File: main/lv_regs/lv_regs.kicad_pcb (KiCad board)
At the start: 2 copper layers, 176 x 67 mm, 53 parts, among them J1 Output, M1 ﻿APXW003A0X3-SRZ, M2 ﻿APXW003A0X3-SRZ, M3 ﻿APXW003A0X3-SRZ

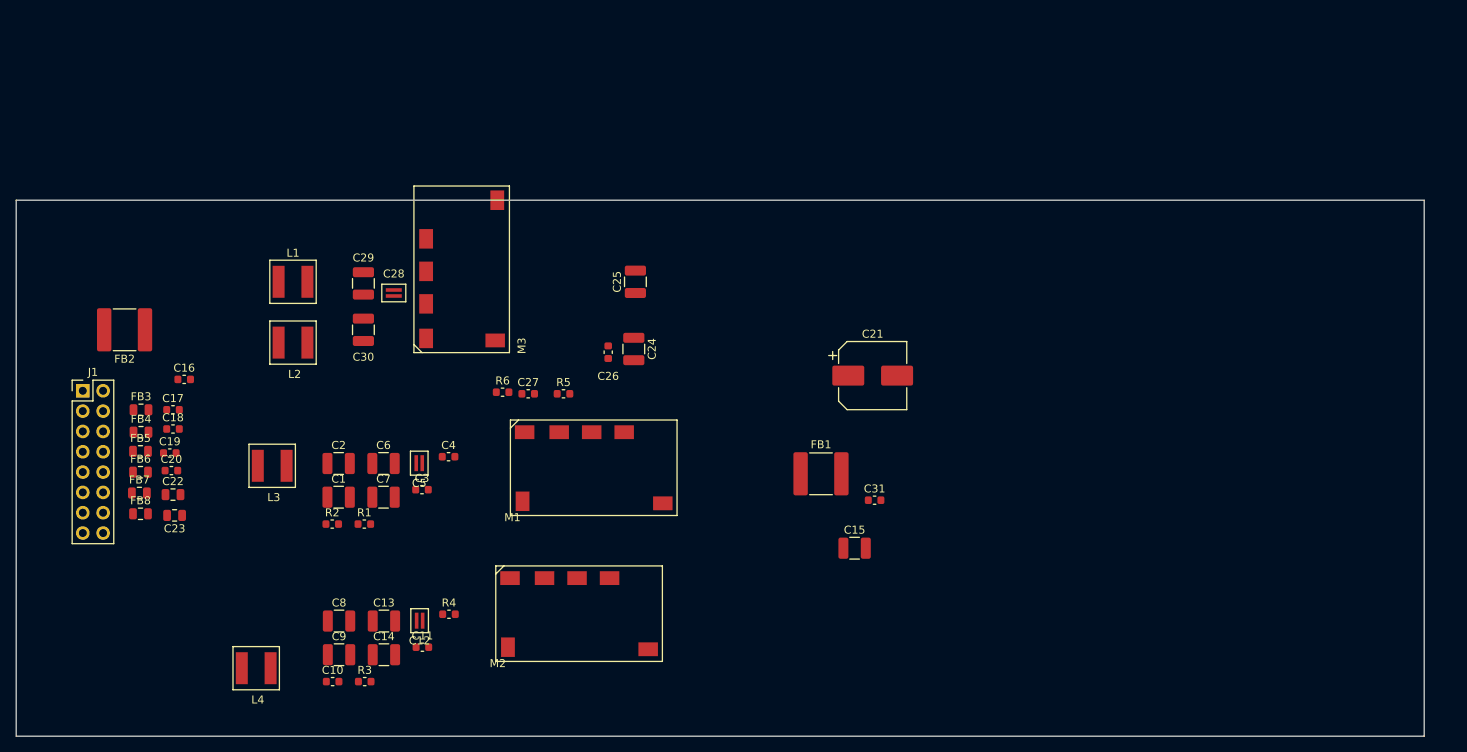
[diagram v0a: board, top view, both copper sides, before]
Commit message: A near final version of the low-volt regulator board. Pending footprint comparison on the actual parts.
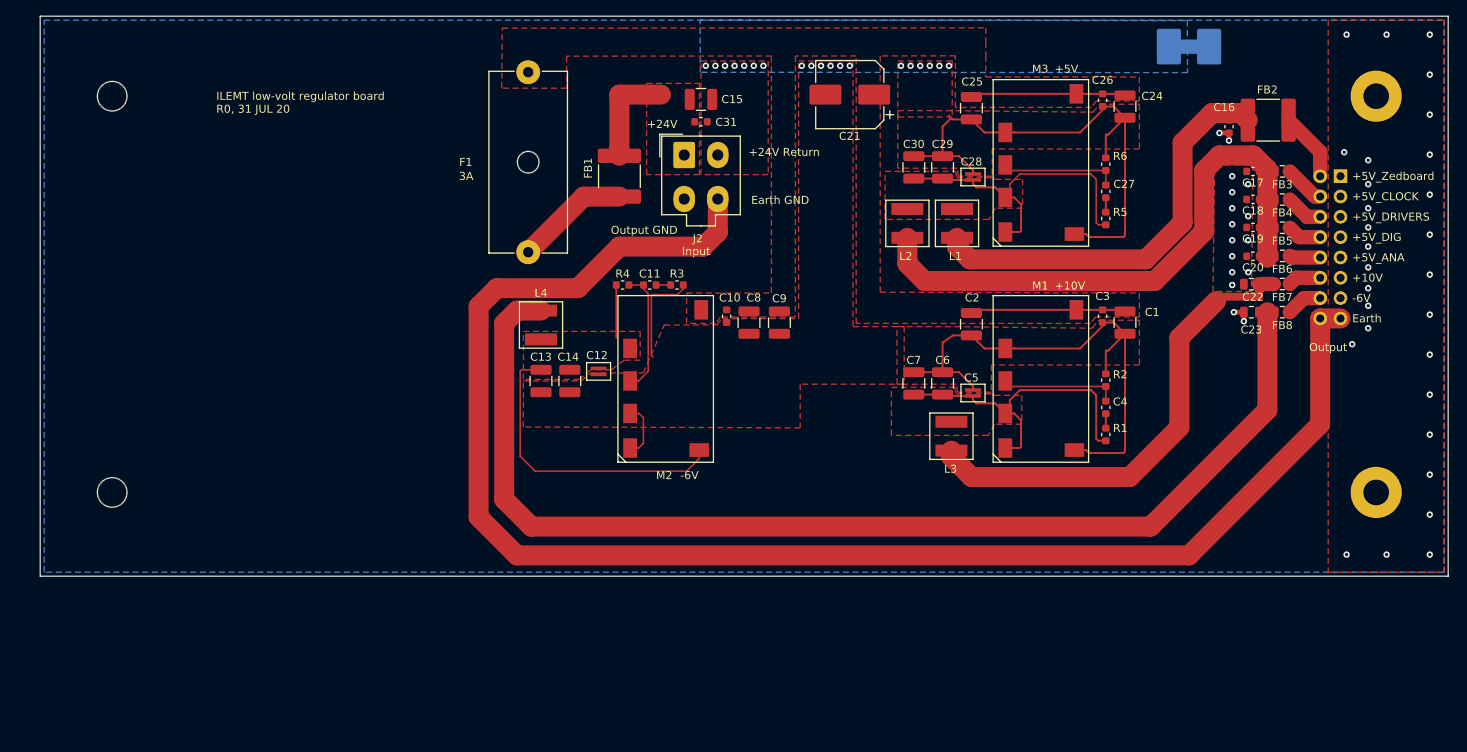
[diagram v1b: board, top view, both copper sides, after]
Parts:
- added F1: 3A, Fuse:Fuseholder_Cylinder-5x20mm_Schurter_0031_8201_Horizontal_Open, F.Cu at (94.0, 47.0)
- added J2: Input, Connector_Molex:Molex_Mini-Fit_Jr_5566-04A_2x02_P4.20mm_Vertical, F.Cu at (113.5, 57.4)
- added MH1: GND, MountingHole:MountingHole_3.2mm_M3_Pad, B.Cu at (200.0, 50.0)
- added MH2: GND, MountingHole:MountingHole_3.2mm_M3_Pad, B.Cu at (200.0, 99.5)
- added R7: DNP, Resistor_SMD:R_2816_7142Metric, B.Cu at (176.6, 43.8)
- added REF**: MountingHole_3.7mm, MountingHole:MountingHole_3.7mm, B.Cu at (42.0, 99.5)
- added REF**: MountingHole_3.7mm, MountingHole:MountingHole_3.7mm, B.Cu at (42.0, 50.0)
- C21: value 330uF -> 100uF
- J1: moved to B.Cu
- moved J1 159.5 mm to (195.5, 60.0), turned to 180 degrees
- moved FB3 145.7 mm to (188.3, 59.4), turned to 180 degrees
- moved FB4 145.6 mm to (188.3, 62.9), turned to 180 degrees
- moved FB5 145.4 mm to (188.3, 66.4), turned to 180 degrees
- moved FB2 145.3 mm to (186.5, 53.0), turned to 0 degrees
- moved FB6 145.3 mm to (188.3, 70.0), turned to 180 degrees
- moved FB7 145.2 mm to (188.3, 73.5), turned to 180 degrees
- moved FB8 144.9 mm to (188.3, 77.0), turned to 180 degrees
- moved C19 138.3 mm to (184.6, 66.4), turned to 180 degrees
- moved C17 138.2 mm to (184.6, 59.4), turned to 180 degrees
- moved C18 138.0 mm to (184.6, 62.9), turned to 180 degrees
- moved C20 137.8 mm to (184.6, 70.0), turned to 180 degrees
- moved C22 137.3 mm to (184.4, 73.5)
- moved C23 137.0 mm to (184.4, 77.0), turned to 0 degrees
- moved C16 134.4 mm to (181.6, 53.8), turned to 270 degrees
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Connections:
- net /reg -5V/VOUT renamed /reg +5V/VOUT
- net Net-(C16-Pad1) renamed /FILT_5V_ZED
- net Net-(C22-Pad2) renamed /FILT_10V
- net Net-(C23-Pad2) renamed /FILT_-6V
- C1 pad 2: GND -> GNDPWR
- C10 pad 2: GND -> GNDPWR
- C12 pad 1: GND -> GNDPWR
- C13 pad 1: GND -> GNDPWR
- C14 pad 1: GND -> GNDPWR
- C15 pad 1: GND -> GNDPWR
- C17 pad 1: Net-(C17-Pad1) -> /FILT_5V_OTHER
- C18 pad 1: Net-(C18-Pad1) -> /FILT_5V_OTHER
- C19 pad 1: Net-(C19-Pad1) -> /FILT_5V_OTHER
- C2 pad 2: GND -> GNDPWR
- C20 pad 1: Net-(C20-Pad1) -> /FILT_5V_OTHER
- C21 pad 2: GND -> GNDPWR
- C24 pad 2: GND -> GNDPWR
- C25 pad 2: GND -> GNDPWR
- C26 pad 2: GND -> GNDPWR
- C28 pad 2: GND -> GNDPWR
- C29 pad 2: GND -> GNDPWR
- C3 pad 2: GND -> GNDPWR
- C30 pad 2: GND -> GNDPWR
- C31 pad 2: GND -> GNDPWR
- C5 pad 2: GND -> GNDPWR
- C6 pad 2: GND -> GNDPWR
- C7 pad 2: GND -> GNDPWR
- C8 pad 2: GND -> GNDPWR
- C9 pad 2: GND -> GNDPWR
- FB1 pad 2: +24V -> Net-(F1-Pad2)
- FB3 pad 2: Net-(C17-Pad1) -> /FILT_5V_OTHER
- FB4 pad 2: Net-(C17-Pad1) -> /FILT_5V_OTHER
- FB5 pad 2: Net-(C17-Pad1) -> /FILT_5V_OTHER
- FB6 pad 2: Net-(C17-Pad1) -> /FILT_5V_OTHER
- L2 pad 1: Net-(C17-Pad1) -> /FILT_5V_OTHER
- M1 pad 1: GND -> GNDPWR
- M1 pad 3: GND -> GNDPWR
- M2 pad 5: GND -> GNDPWR
- M2 pad 6: GND -> GNDPWR
- M3 pad 1: GND -> GNDPWR
- M3 pad 3: GND -> GNDPWR
- R2 pad 2: GND -> GNDPWR
- R3 pad 1: GND -> GNDPWR
- R6 pad 2: GND -> GNDPWR
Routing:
- net Earth: track 0.00 -> 194.0 mm
- net GNDPWR: track 0.00 -> 153.9 mm, vias 0 -> 19
- net /FILT_-6V: track 0.00 -> 142.3 mm
- net /FILT_5V_OTHER: track 0.00 -> 71.9 mm
- net /FILT_10V: track 0.00 -> 59.6 mm
- net /FILT_5V_ZED: track 0.00 -> 51.9 mm
- net /reg -6V/VOUT: track 0.00 -> 44.8 mm
- net /reg +5V/VOUT: track 0.00 -> 40.5 mm
- net /reg +10V/VOUT: track 0.00 -> 40.5 mm
- net +24V: track 0.00 -> 38.9 mm
- net Net-(C11-Pad2): track 0.00 -> 15.6 mm
- net Net-(C4-Pad2): track 0.00 -> 14.8 mm
- net Net-(C27-Pad2): track 0.00 -> 14.8 mm
- net Net-(F1-Pad2): track 0.00 -> 14.3 mm
- net Net-(C15-Pad2): track 0.00 -> 12.8 mm
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- added copper zone on F.Cu, net +24V
- added copper zone on F.Cu, net /reg +10V/VOUT
- added copper zone on F.Cu, net /reg +5V/VOUT
- added copper zone on F.Cu, net /reg -6V/VOUT
- added copper zone on B.Cu, net GND
- added copper zone on F.Cu, net GND
- added copper zone on B.Cu, net GNDPWR
- added copper zone on F.Cu, net GNDPWR
- added copper zone on F.Cu, net Net-(C15-Pad2)
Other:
- board size 176 x 67 mm -> 176 x 70 mm
- board text added: "+10V"
- board text added: "+24V"
- board text added: "+24V Return"
- board text added: "+5V"
- board text added: "+5V_ANA"
- board text added: "+5V_CLOCK"
- board text added: "+5V_DIG"
- board text added: "+5V_DRIVERS"
- board text added: "+5V_Zedboard"
- board text added: "-6V"
- board text added: "Bottom layer is output ground (GND), a shield, not a plane. It is not tied anywhere but at the output connector and the GND line on the input connector."
- board text added: "Earth"
- board text added: "Earth GND"
- board text added: "ILEMT low-volt regulator board R0, 31 JUL 20"
- board text added: "Output"
- board text added: "Output GND"
- board text added: "This board is mounted bottom-to-bottom with the main board, so it appears flipped left-to-right. The mating output connector pins are also interchanged even-for-odd because of this."
